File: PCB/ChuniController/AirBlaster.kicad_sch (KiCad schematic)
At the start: 0 parts

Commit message: PCB
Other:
- sheet IRBlaster ports: added 5V; removed 3V3
- sheet IRBlaster1 ports: added 5V; removed 3V3
- sheet IRBlaster2 ports: added 5V; removed 3V3
- sheet IRBlaster3 ports: added 5V; removed 3V3
- sheet IRBlaster4 ports: added 5V; removed 3V3
- sheet IRBlaster5 ports: added 5V; removed 3V3
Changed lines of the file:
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@@
-	)
-	(bus_entry
-		(at 38.1 154.94)
-		(size -2.54 -2.54)
-		(stroke
-			(width 0)
-			(type default)
-		)
 	)
 	(bus_entry
@@
 		)
 	)
-	(bus_entry
-		(at 38.1 161.29)
-		(size -2.54 -2.54)
-		(stroke
-			(width 0)
-			(type default)
-		)
-	)
 	(wire
 		(pts
@@
 	(wire
 		(pts
-			(xy 33.02 128.27) (xy 33.02 156.21)
-		)
-		(stroke
-			(width 0)
-			(type default)
-		)
-	)
-	(wire
-		(pts
 			(xy 33.02 45.72) (xy 33.02 62.23)
 		)
@@
 	(wire
 		(pts
+			(xy 33.02 128.27) (xy 33.02 161.29)
+		)
+		(stroke
+			(width 0)
+			(type default)
+		)
+	)
+	(wire
+		(pts
 			(xy 35.56 106.68) (xy 35.56 123.19)
 		)
@@
 	(wire
 		(pts
-			(xy 35.56 158.75) (xy 33.02 156.21)
-		)
-		(stroke
-			(width 0)
-			(type default)
-		)
-	)
-	(wire
-		(pts
 			(xy 40.64 109.22) (xy 50.8 109.22)
 		)
@@
 	(wire
 		(pts
+			(xy 35.56 123.19) (xy 35.56 161.29)
+		)
+		(stroke
+			(width 0)
+			(type default)
+		)
+	)
+	(wire
+		(pts
 			(xy 35.56 57.15) (xy 50.8 57.15)
 		)
@@
 		(pts
 			(xy 35.56 73.66) (xy 35.56 90.17)
-		)
-		(stroke
-			(width 0)
-			(type default)
-		)
-	)
-	(wire
-		(pts
-			(xy 35.56 123.19) (xy 35.56 152.4)
 		)
 		(stroke
@@
 		)
 	)
-	(label "GND"
-		(at 33.02 156.21 0)
-		(effects
-			(font
-				(size 1.27 1.27)
-			)
-			(justify left bottom)
-		)
-	)
 	(label "EMIT5"
 		(at 40.64 109.22 0)
@@
 		)
 	)
-	(label "3V3"
-		(at 35.56 152.4 0)
-		(effects
-			(font
-				(size 1.27 1.27)
-			)
-			(justify left bottom)
-		)
-	)
 	(label "EMIT2"
 		(at 40.64 59.69 0)
@@
 		)
 	)
-	(hierarchical_label "{3V3 GND EMIT[1..6] SENSE[1..6]}"
+	(hierarchical_label "{EMIT[1..6]}"
 		(shape bidirectional)
 		(at 38.1 161.29 270)
+		(effects
+			(font
+				(size 1.27 1.27)
+			)
+			(justify right)
+		)
+	)
+	(hierarchical_label "GND"
+		(shape output)
+		(at 33.02 161.29 270)
+		(effects
+			(font
+				(size 1.27 1.27)
+			)
+			(justify right)
+		)
+	)
+	(hierarchical_label "5V"
+		(shape input)
+		(at 35.56 161.29 270)
 		(effects
 			(font
@@
 			)
 		)
-		(pin "3V3" input
+		(pin "5V" input
 			(at 50.8 90.17 180)
 			(effects
@@
 			)
 		)
-		(pin "3V3" input
+		(pin "5V" input
 			(at 50.8 57.15 180)
 			(effects
@@
 			)
 		)
-		(pin "3V3" input
+		(pin "5V" input
 			(at 50.8 106.68 180)
 			(effects
@@
 			)
 		)
-		(pin "3V3" input
-			(at 50.8 123.19 180)
-			(effects
-				(font
-					(size 1.27 1.27)
-				)
-				(justify left)
-			)
-		)
 		(pin "SIG" input
 			(at 50.8 125.73 180)
@@
 		(pin "GND" output
 			(at 50.8 128.27 180)
+			(effects
+				(font
+					(size 1.27 1.27)
+				)
+				(justify left)
+			)
+		)
+		(pin "5V" input
+			(at 50.8 123.19 180)
 			(effects
 				(font
@@
 			)
 		)
-		(pin "3V3" input
+		(pin "5V" input
 			(at 50.8 73.66 180)
 			(effects
@@
 			)
 		)
-		(pin "3V3" input
+		(pin "5V" input
 			(at 50.8 40.64 180)
 			(effects

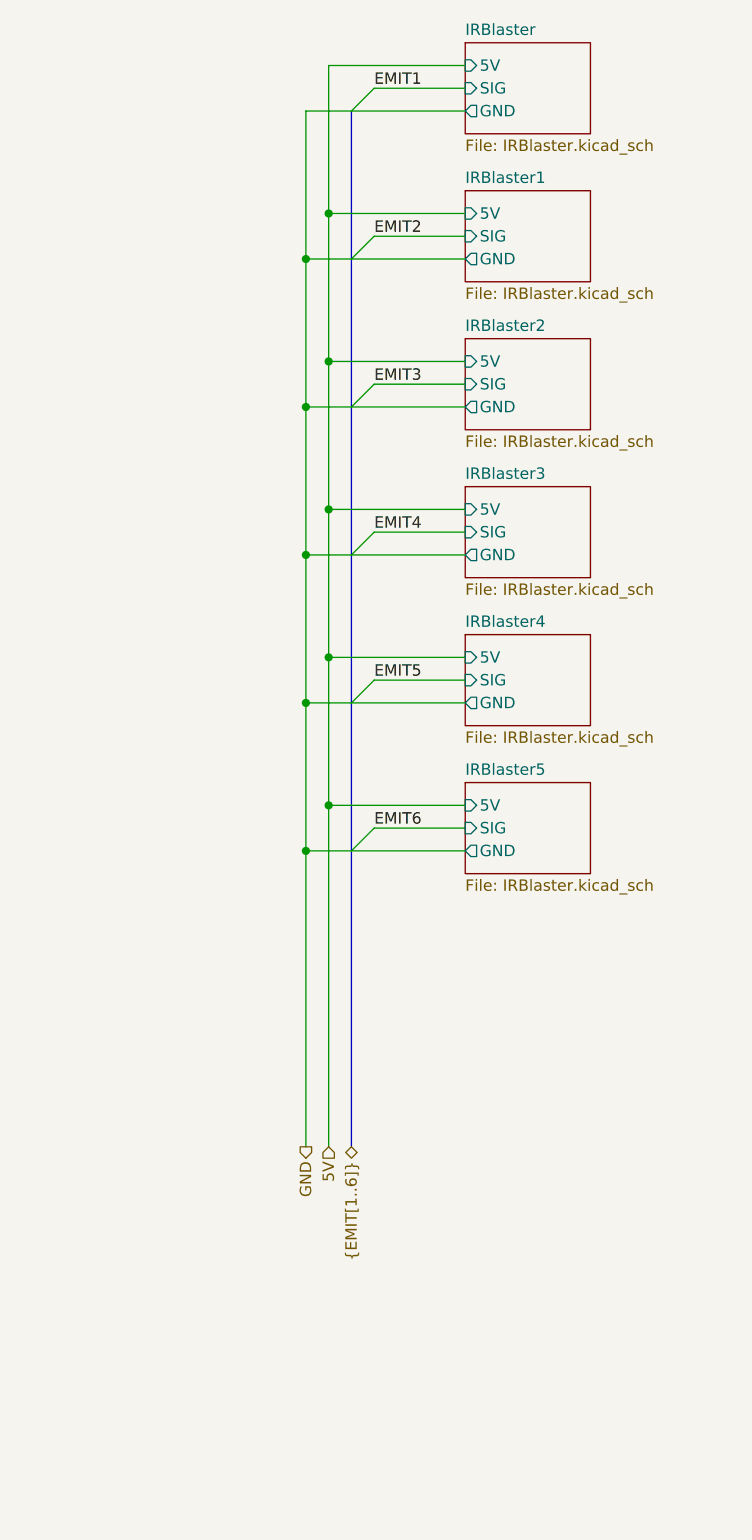
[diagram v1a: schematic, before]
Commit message: PCB both ir board: ok add LM393D 3d model
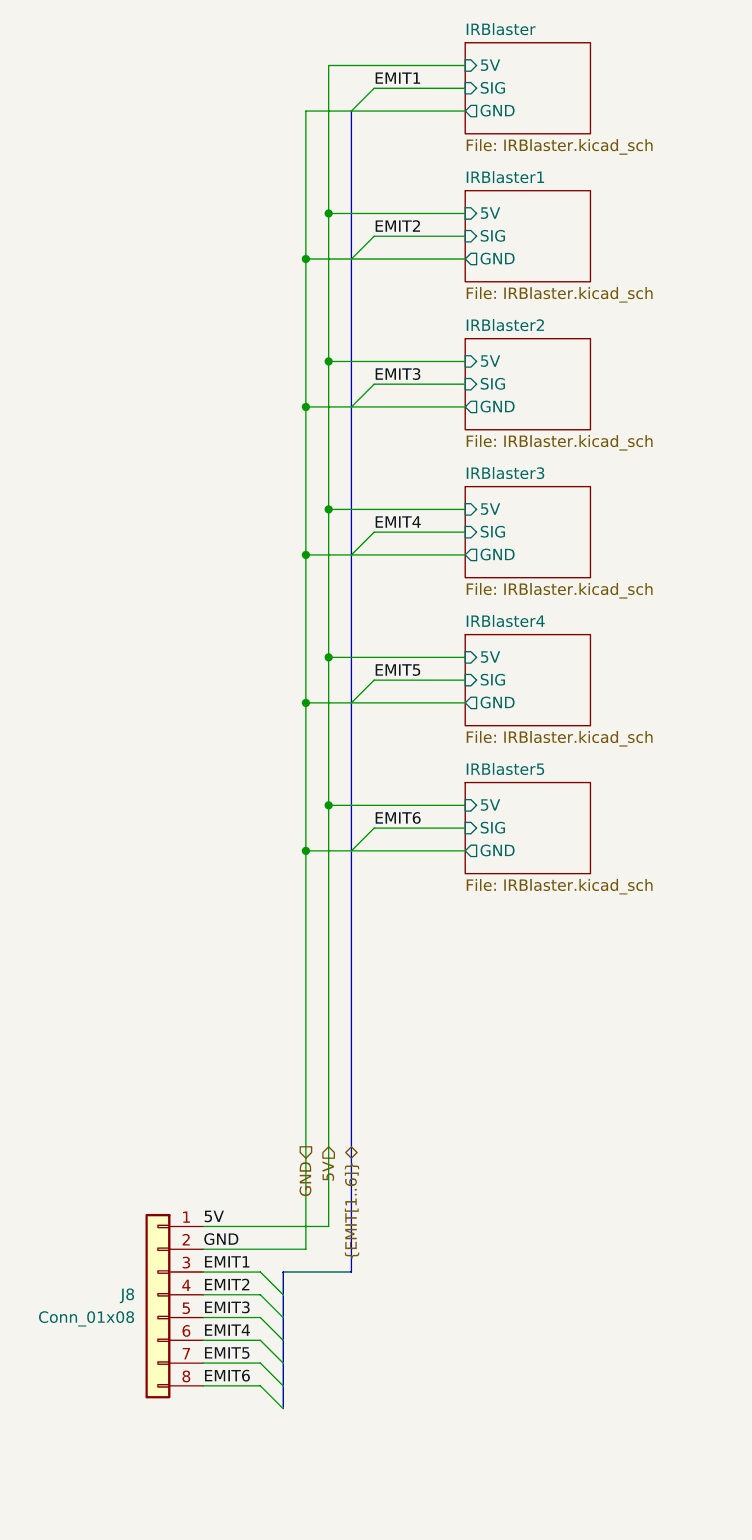
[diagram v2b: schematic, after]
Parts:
- added J8: Conn_01x08, Connector_JST:JST_SH_SM08B-SRSS-TB_1x08-1MP_P1.00mm_Horizontal, symbol Connector_Generic:Conn_01x08
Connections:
- net 5V: now also J8.1 (Pin_1)
- net EMIT1: now also J8.3 (Pin_3)
- net EMIT2: now also J8.4 (Pin_4)
- net EMIT3: now also J8.5 (Pin_5)
- net EMIT4: now also J8.6 (Pin_6)
- net EMIT5: now also J8.7 (Pin_7)
- net EMIT6: now also J8.8 (Pin_8)
- net GND: now also J8.2 (Pin_2)

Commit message: PCB
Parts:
- removed J8: Conn_01x08, Connector_JST:JST_SH_SM08B-SRSS-TB_1x08-1MP_P1.00mm_Horizontal, symbol Connector_Generic:Conn_01x08
